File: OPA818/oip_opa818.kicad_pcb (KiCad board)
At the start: 2 copper layers, 25 x 25 mm, 35 parts, among them J101 Conn_Coaxial, J102 Conn_01x03, U101 LT3042xMSE, U102 LT3093xMSE, U103 OPA818IDRGx, U104 BUF602xDBV

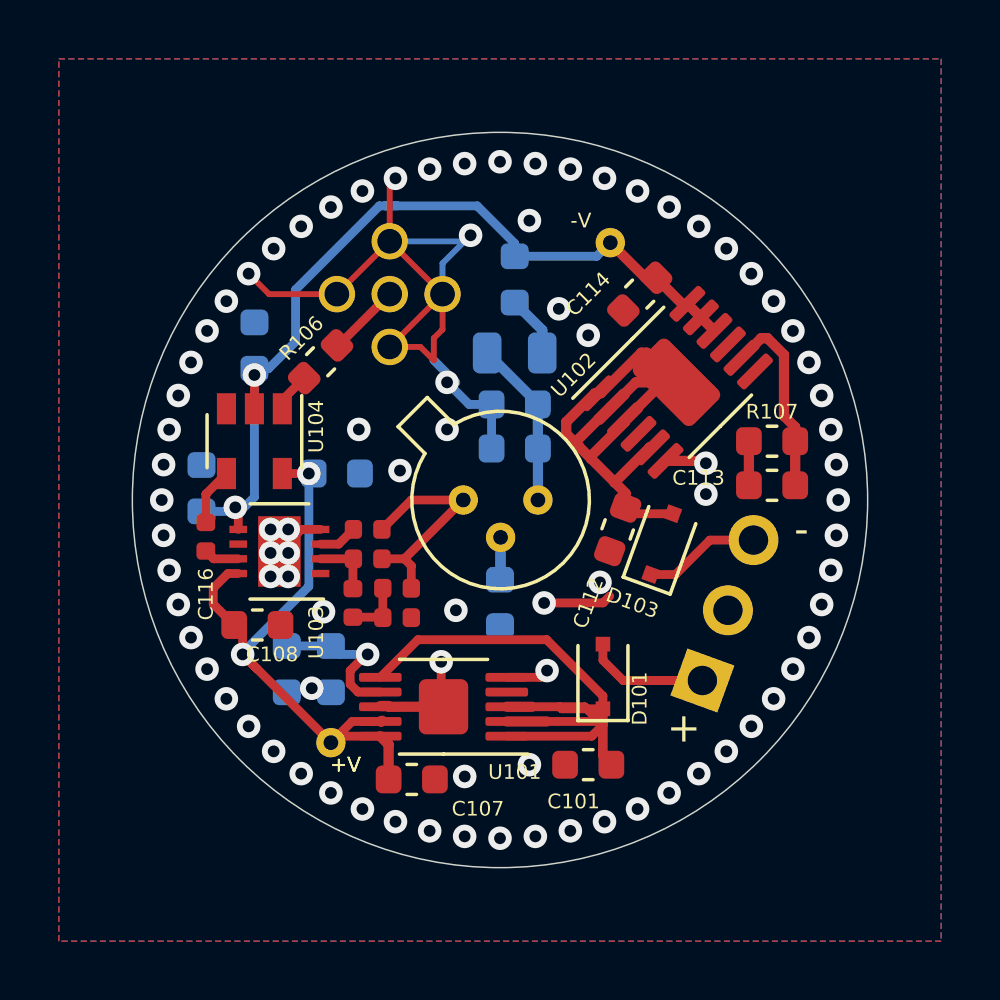
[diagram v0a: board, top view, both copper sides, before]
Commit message: add bom
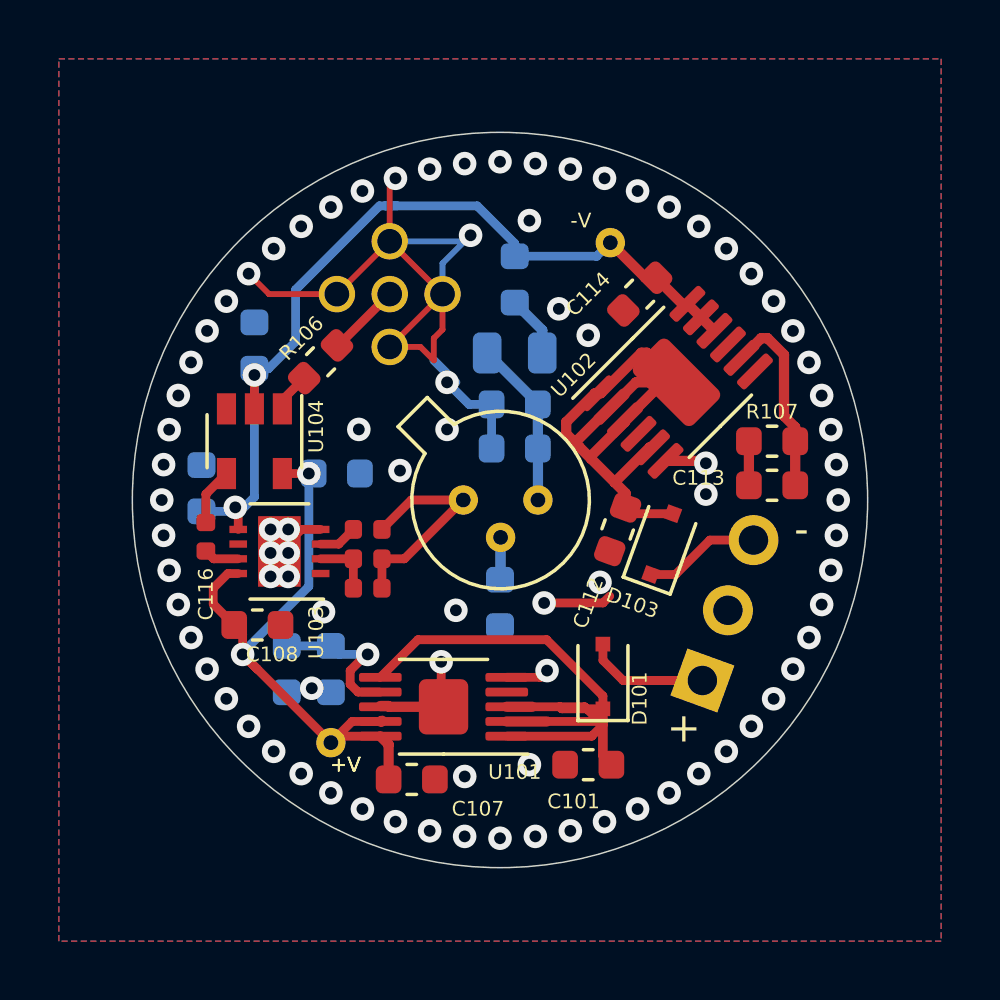
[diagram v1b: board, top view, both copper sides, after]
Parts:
- removed C110, C111: C, Capacitor_SMD:C_0402_1005Metric
- moved C115 1.00 mm to (145.5, 103.0)
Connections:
- C115 pad 1: Net-(C110-Pad1) -> /FB
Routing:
- net Net-(C110-Pad1): track 2.02 -> 0.00 mm
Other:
- rule pad_to_mask_clearance: 0.051 -> 0

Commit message: move all parts to top side of pcb
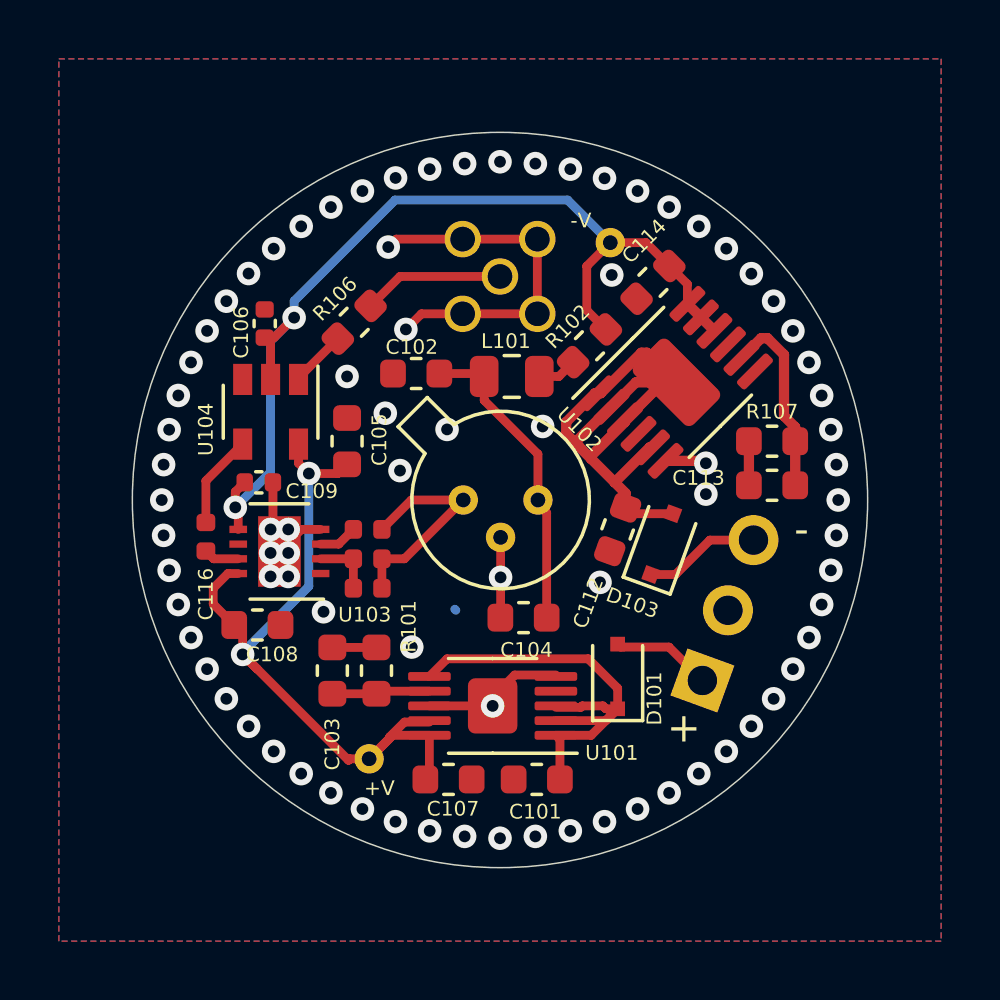
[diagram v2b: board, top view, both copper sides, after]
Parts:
- removed R103: 0R, Resistor_SMD:R_0603_1608Metric
- C102, C103, C104, C105, L101, R102: moved to F.Cu
- C106, C109: footprint Capacitor_SMD:C_0603_1608Metric -> Capacitor_SMD:C_0402_1005Metric; moved to F.Cu
- R101: value 25k -> 56k; moved to F.Cu
- R107: value 25k -> 56k
- moved C104 5.76 mm to (150.8, 104.0)
- moved J101 3.80 mm to (150.0, 92.4), turned to 0 degrees
- moved C102 3.51 mm to (147.2, 95.7)
- moved R102 3.40 mm to (153.0, 94.8), turned to 225 degrees
- moved C109 1.96 mm to (141.8, 99.4), turned to 0 degrees
- moved C101 1.82 mm to (151.2, 109.5)
- moved R106 1.76 mm to (145.0, 94.0)
- moved U101 1.67 mm to (149.8, 107.0)
- moved C103 1.55 mm to (144.3, 105.8), turned to 90 degrees
- moved R101 1.55 mm to (145.8, 105.8), turned to 90 degrees
- moved TP102 1.41 mm to (145.6, 108.8)
- moved C107 1.25 mm to (148.2, 109.5)
- moved C105 1.15 mm to (144.8, 98.0), turned to 270 degrees
- moved U104 1.14 mm to (142.2, 97.0)
- moved C106 0.83 mm to (142.0, 94.0)
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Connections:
- D102 pad 2: Net-(D102-Pad2) -> GND
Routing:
- net GND: track 39.5 -> 28.2 mm, vias 85 -> 81
- net Net-(C101-Pad1): track 27.0 -> 16.2 mm
- net /+V: track 21.8 -> 27.3 mm
- net /VBIAS: track 5.72 -> 10.6 mm
- net /-V: track 29.9 -> 34.1 mm
- net Net-(D102-Pad2): track 2.94 -> 0.00 mm
- net Net-(J101-Pad1): track 2.52 -> 4.81 mm
- net /+VIN: track 5.66 -> 3.39 mm
- net /SET+: track 5.29 -> 3.34 mm, vias 1 -> 0
- net Net-(C116-Pad2): track 1.95 -> 3.18 mm
- net Net-(L101-Pad1): track 2.10 -> 1.35 mm
- net /VOUT: track 1.35 -> 1.99 mm
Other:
- net class Default: clearance 0.25 -> 0.15
- net class PWR: clearance 0.25 -> 0.15
- rule trace_clearance: 0.25 -> 0.15

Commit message: docs
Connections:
- net /VBIAS renamed /-5VBIAS

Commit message: v6
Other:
- net class Default removed
- net class PWR removed
